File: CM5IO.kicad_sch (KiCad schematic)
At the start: 41 parts, among them J1 703W-00_53, J10 691210910004, J2 B2B-PH-K-S, J3 B2B-PH-K-S, J4 VR10S09, J5 691101810005, J6 691210910006, J7 691210910006, J8 5055750471, J9 1726470103, U1 UWS-5_10-Q48N-C, U14 CDCLVC1106PWR, U15 CDCLVC1106PWR, U2 RCLAMP3354S.TCT

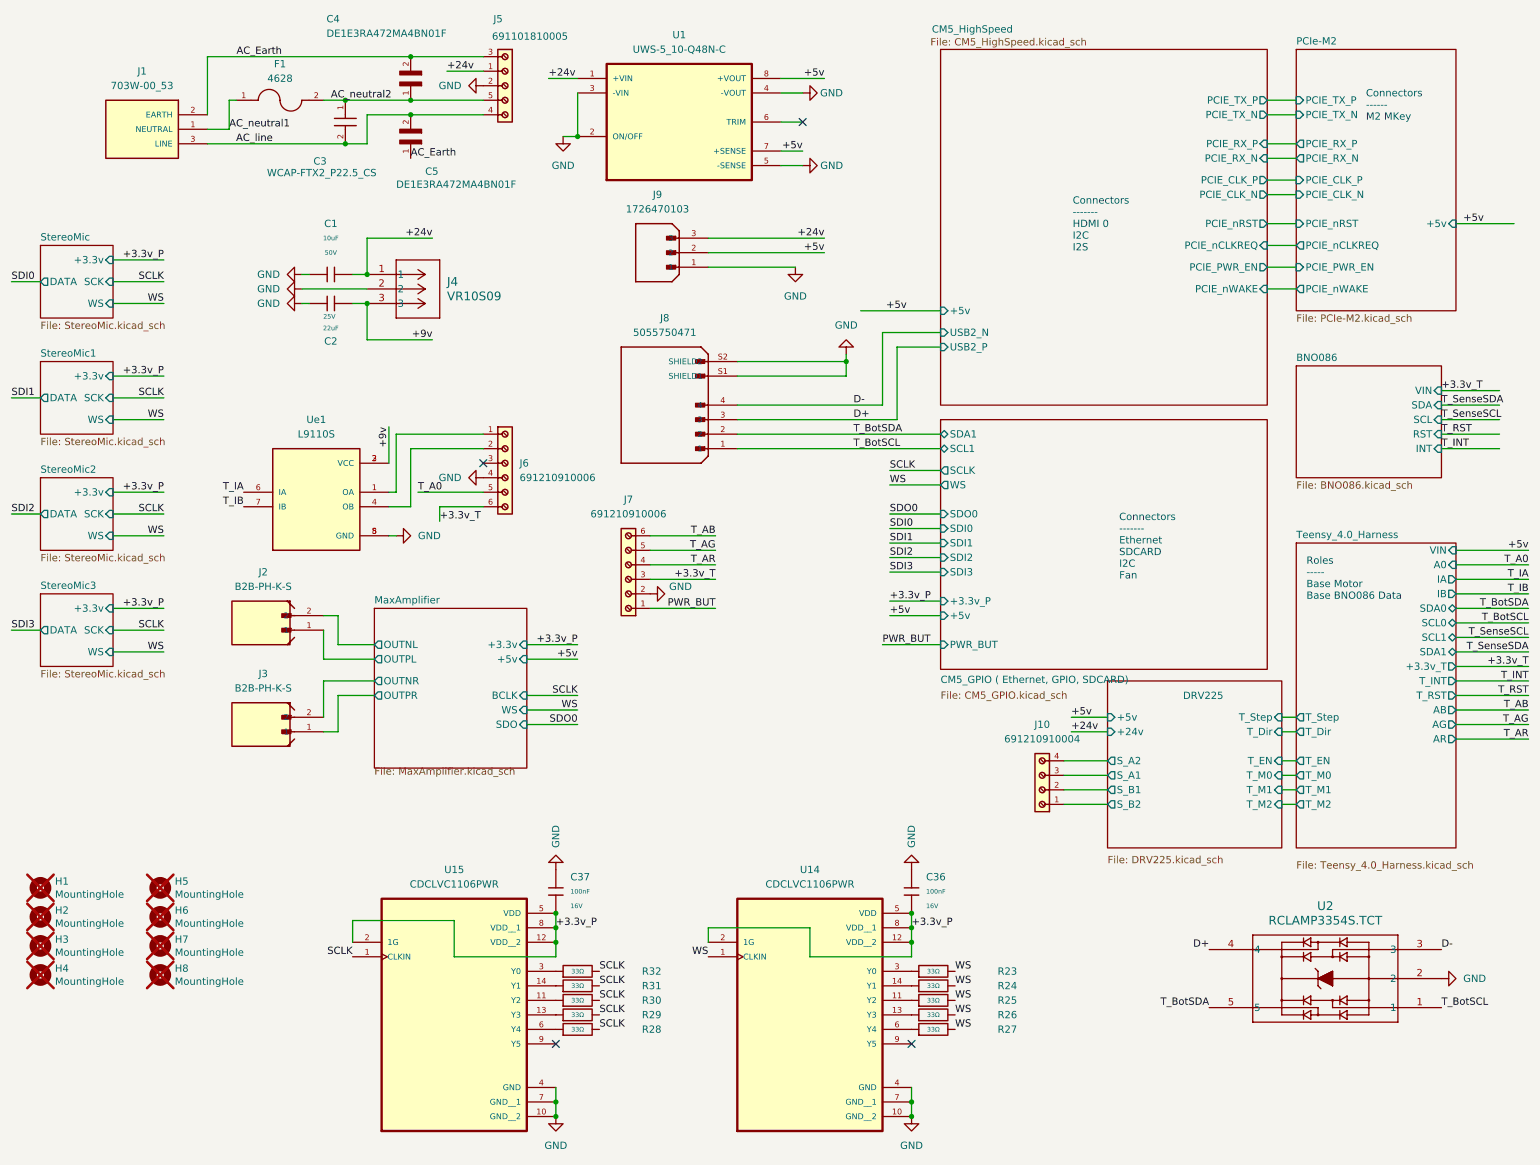
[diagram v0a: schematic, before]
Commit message: deletes power and vestigial connectors
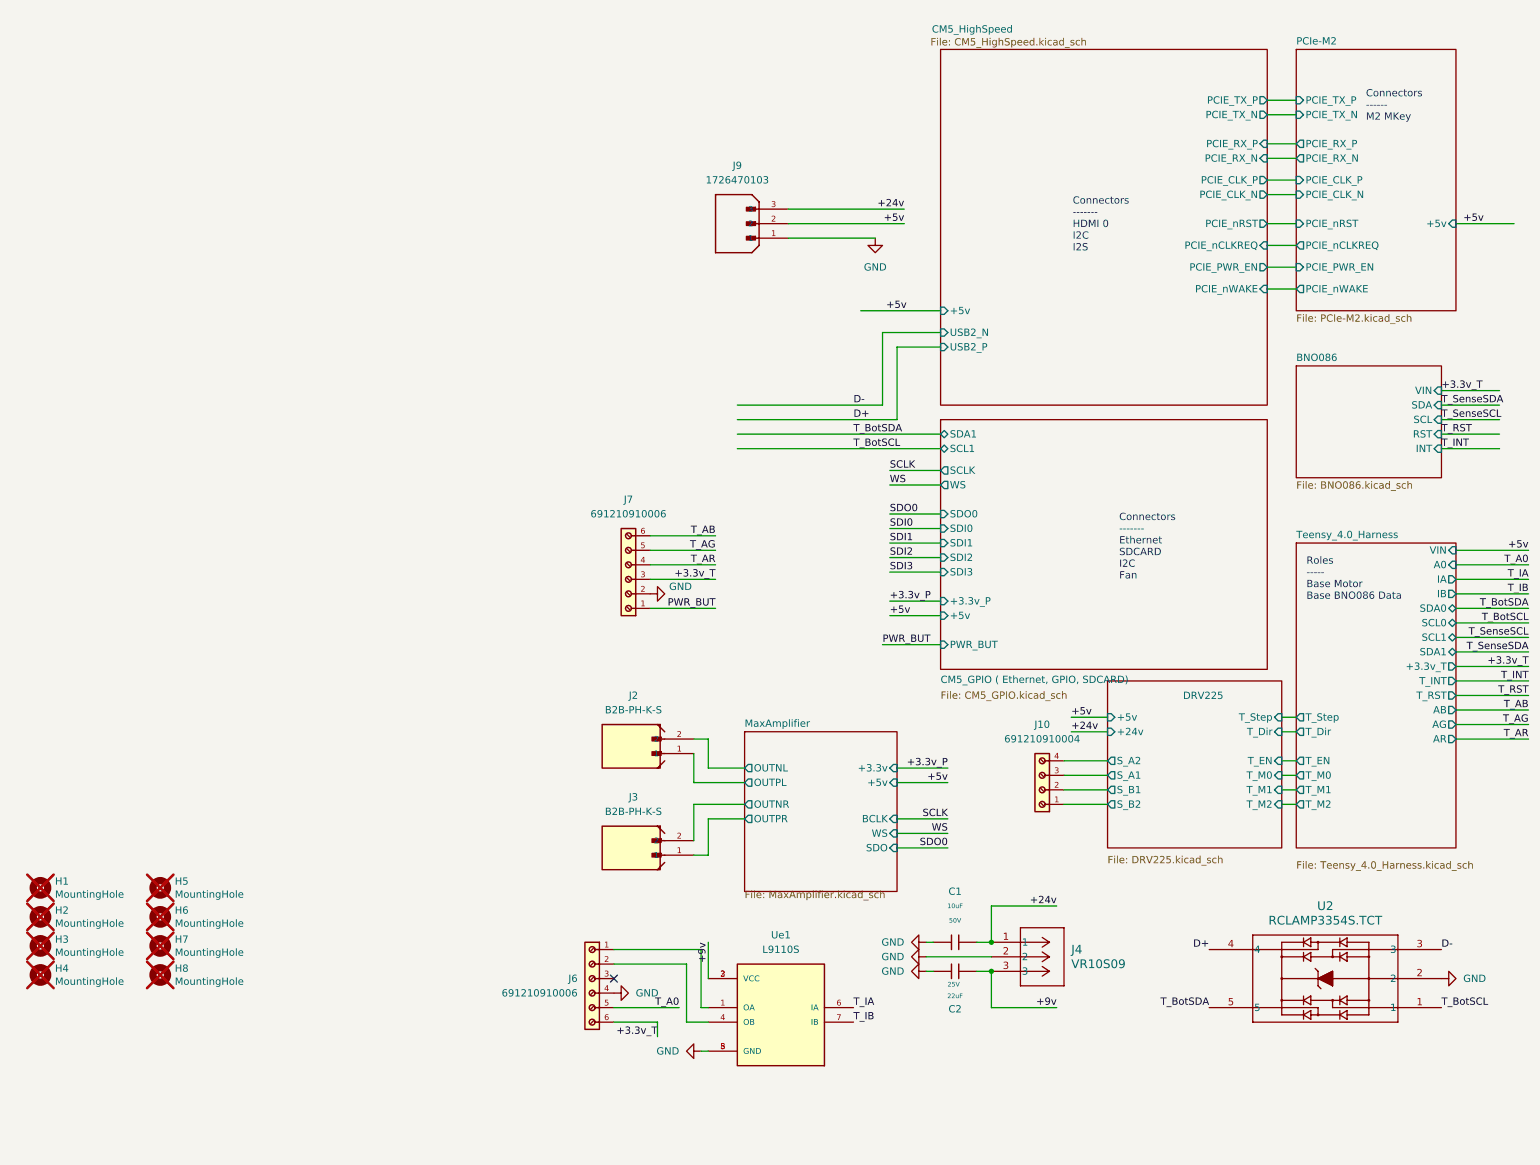
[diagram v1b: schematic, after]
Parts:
- removed C3: WCAP-FTX2_P22.5_CS, Custom Components:WCAP-FTX2_P22.5L26W6H12_CS, symbol WCAP-FTX2_P22.5_CS:WCAP-FTX2_P22.5_CS
- removed C36, C37: 100nF, PCM_JLCPCB:C_0402, symbol PCM_JLCPCB-Capacitors:0402,100nF
- removed C4, C5: DE1E3RA472MA4BN01F, Custom Components:CAP_DE1E3RA472MA4BN01F, symbol DE1E3RA472MA4BN01F:DE1E3RA472MA4BN01F
- removed F1: 4628, Custom Components:FUSE_4628, symbol 4628:4628
- removed J1: 703W-00_53, Custom Components:QUALTEK_703W-00_53, symbol 703W-00_53:703W-00_53
- removed J5: 691101810005, Custom Components:691101810005, symbol 691101810005:691101810005
- removed J8: 5055750471, Custom Components:MOLEX_5055750471, symbol 5055750471:5055750471
- removed R23, R24, R25, R26, R27, R28, R29, R30, R31, R32: 33Ω, PCM_JLCPCB:R_0402, symbol PCM_JLCPCB-Resistors:0402,33Ω
- removed U1: UWS-5_10-Q48N-C, Custom Components:VREG_UWS-5_10-Q48N-C, symbol UWS-5_10-Q48N-C:UWS-5_10-Q48N-C
- removed U14, U15: CDCLVC1106PWR, Custom Components:SOP65P640X120-14N, symbol CDCLVC1106PWR:CDCLVC1106PWR
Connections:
- no-connect marks 4 -> 1
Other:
- removed sheet StereoMic
- removed sheet StereoMic1
- removed sheet StereoMic2
- removed sheet StereoMic3
- moved on the sheet: C1, C2, J2, J3, J4, J6, J9, Ue1
